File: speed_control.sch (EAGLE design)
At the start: 3 parts

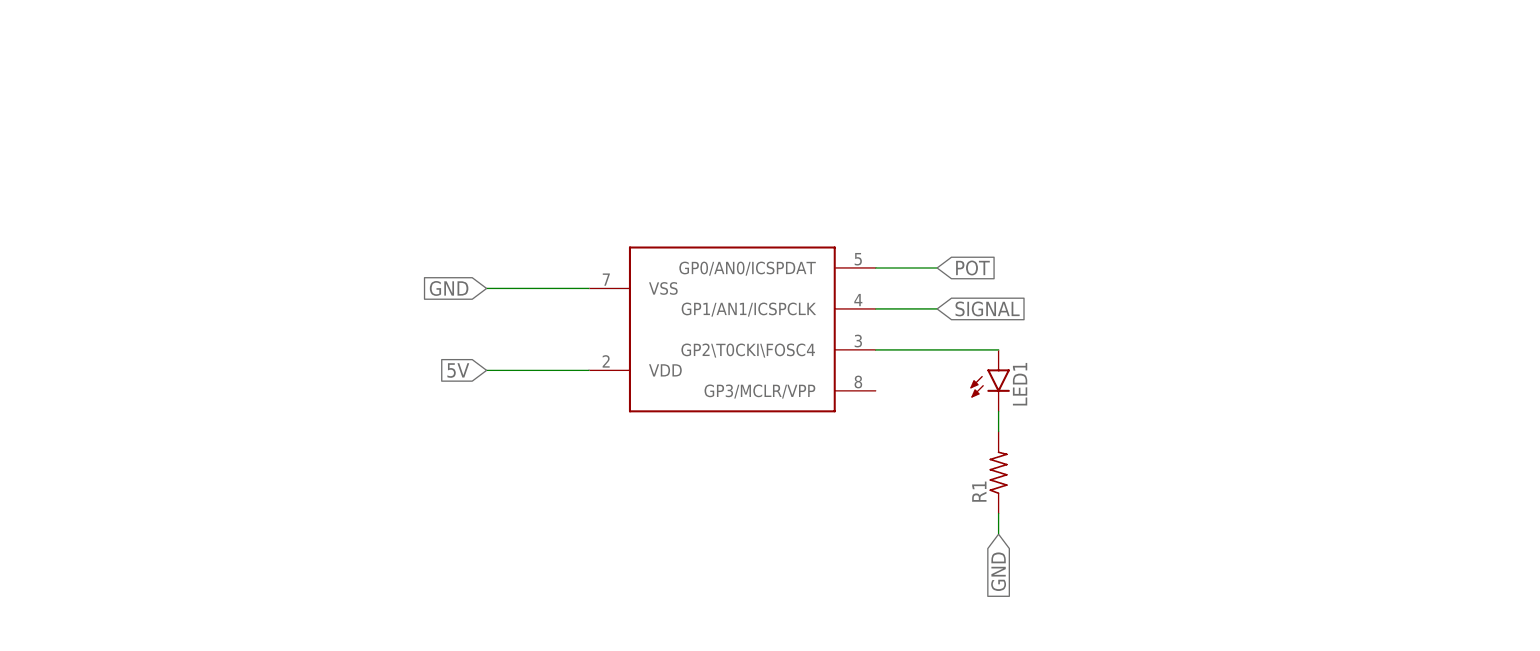
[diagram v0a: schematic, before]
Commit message: Added headers to circuit
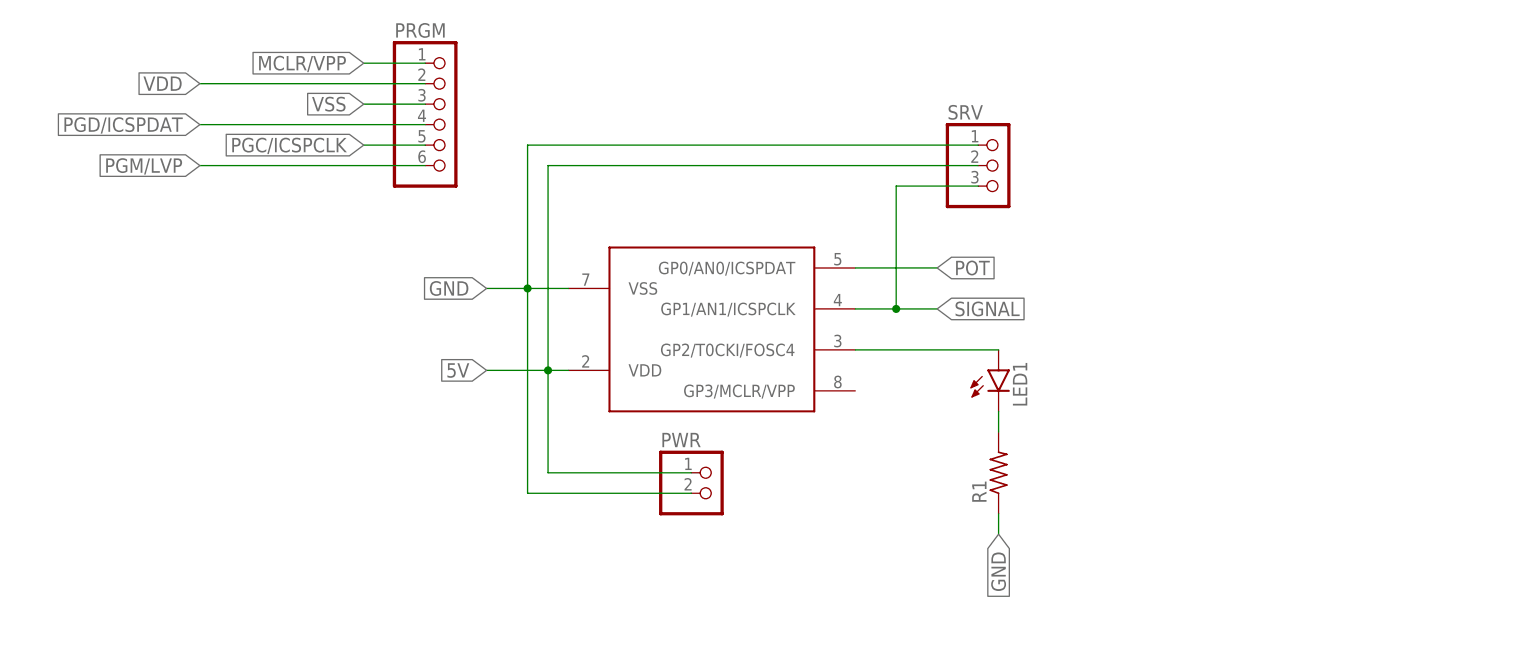
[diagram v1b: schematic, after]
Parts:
- added PRGM: (no value), pinhead:PINHD-1X6/90
- added PWR: (no value), pinhead:PINHD-1X2/90
- added SRV: (no value), pinhead:PINHD-1X3/90
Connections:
- new net MCLR/VPP: PRGM.1
- new net PGC/ICSPCLK: PRGM.5
- new net PGD/ICSPDAT: PRGM.4
- new net PGM/LVP: PRGM.6
- new net VDD: PRGM.2
- new net VSS: PRGM.3
- net 5V: now also PWR.1, SRV.2
- net GND: now also PWR.2, SRV.1
- net N$1: now also U$1.GP2/T0CKI/FOSC4; no longer U$1.GP2\T0CKI\FOSC4
- net SIGNAL: now also SRV.3
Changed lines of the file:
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@@
 </classes>
 <parts>
-<part name="U$1" library="PIC10F222" deviceset="PIC10F222" device="PIC10F222" package3d_urn="urn:adsk.eagle:package:16702925/1"/>
 <part name="LED1" library="led" library_urn="urn:adsk.eagle:library:259" deviceset="LED" device="3MM" package3d_urn="urn:adsk.eagle:package:15797/1"/>
 <part name="R1" library="rcl" library_urn="urn:adsk.eagle:library:334" deviceset="R-US_" device="0207/10" package3d_urn="urn:adsk.eagle:package:23491/2"/>
+<part name="SRV" library="pinhead" library_urn="urn:adsk.eagle:library:325" deviceset="PINHD-1X3" device="/90" package3d_urn="urn:adsk.eagle:package:22459/2"/>
+<part name="PWR" library="pinhead" library_urn="urn:adsk.eagle:library:325" deviceset="PINHD-1X2" device="/90" package3d_urn="urn:adsk.eagle:package:22437/2"/>
+<part name="PRGM" library="pinhead" library_urn="urn:adsk.eagle:library:325" deviceset="PINHD-1X6" device="/90" package3d_urn="urn:adsk.eagle:package:22475/2"/>
+<part name="U$1" library="PIC10F222" deviceset="PIC10F222" device="PIC10F222" package3d_urn="urn:adsk.eagle:package:16702925/1"/>
 </parts>
 <sheets>
@@
 </plain>
 <instances>
-<instance part="U$1" gate="G$1" x="-2.54" y="-7.62" smashed="yes"/>
 <instance part="LED1" gate="G$1" x="33.02" y="-5.08" smashed="yes">
 <attribute name="NAME" x="36.576" y="-9.652" size="1.778" layer="95" rot="R90"/>
@@
 <attribute name="VALUE" x="36.322" y="-21.59" size="1.778" layer="96" rot="R90"/>
 </instance>
+<instance part="SRV" gate="A" x="33.02" y="20.32" smashed="yes">
+<attribute name="NAME" x="26.67" y="26.035" size="1.778" layer="95"/>
+<attribute name="VALUE" x="26.67" y="12.7" size="1.778" layer="96"/>
+</instance>
+<instance part="PWR" gate="G$1" x="-2.54" y="-20.32" smashed="yes">
+<attribute name="NAME" x="-8.89" y="-14.605" size="1.778" layer="95"/>
+<attribute name="VALUE" x="-8.89" y="-25.4" size="1.778" layer="96"/>
+</instance>
+<instance part="PRGM" gate="A" x="-35.56" y="25.4" smashed="yes">
+<attribute name="NAME" x="-41.91" y="36.195" size="1.778" layer="95"/>
+<attribute name="VALUE" x="-41.91" y="15.24" size="1.778" layer="96"/>
+</instance>
+<instance part="U$1" gate="G$1" x="-2.54" y="0" smashed="yes"/>
 </instances>
 <busses>
@@
 <net name="GND" class="0">
 <segment>
+<wire x1="-20.32" y1="5.08" x2="-25.4" y2="5.08" width="0.1524" layer="91"/>
+<label x="-30.48" y="5.08" size="1.778" layer="95" rot="R180" xref="yes"/>
+<pinref part="PWR" gate="G$1" pin="2"/>
+<wire x1="-25.4" y1="5.08" x2="-30.48" y2="5.08" width="0.1524" layer="91"/>
+<wire x1="-5.08" y1="-20.32" x2="-25.4" y2="-20.32" width="0.1524" layer="91"/>
+<wire x1="-25.4" y1="-20.32" x2="-25.4" y2="5.08" width="0.1524" layer="91"/>
+<junction x="-25.4" y="5.08"/>
+<wire x1="-25.4" y1="5.08" x2="-25.4" y2="22.86" width="0.1524" layer="91"/>
+<pinref part="SRV" gate="A" pin="1"/>
+<wire x1="-25.4" y1="22.86" x2="30.48" y2="22.86" width="0.1524" layer="91"/>
 <pinref part="U$1" gate="G$1" pin="VSS"/>
-<wire x1="-17.78" y1="5.08" x2="-30.48" y2="5.08" width="0.1524" layer="91"/>
-<label x="-30.48" y="5.08" size="1.778" layer="95" rot="R180" xref="yes"/>
 </segment>
 <segment>
@@
 <net name="5V" class="0">
 <segment>
+<wire x1="-20.32" y1="-5.08" x2="-22.86" y2="-5.08" width="0.1524" layer="91"/>
+<label x="-30.48" y="-5.08" size="1.778" layer="95" rot="R180" xref="yes"/>
+<pinref part="PWR" gate="G$1" pin="1"/>
+<wire x1="-22.86" y1="-5.08" x2="-30.48" y2="-5.08" width="0.1524" layer="91"/>
+<wire x1="-5.08" y1="-17.78" x2="-22.86" y2="-17.78" width="0.1524" layer="91"/>
+<wire x1="-22.86" y1="-17.78" x2="-22.86" y2="-5.08" width="0.1524" layer="91"/>
+<junction x="-22.86" y="-5.08"/>
+<wire x1="-22.86" y1="-5.08" x2="-22.86" y2="20.32" width="0.1524" layer="91"/>
+<pinref part="SRV" gate="A" pin="2"/>
+<wire x1="-22.86" y1="20.32" x2="30.48" y2="20.32" width="0.1524" layer="91"/>
 <pinref part="U$1" gate="G$1" pin="VDD"/>
-<wire x1="-17.78" y1="-5.08" x2="-30.48" y2="-5.08" width="0.1524" layer="91"/>
-<label x="-30.48" y="-5.08" size="1.778" layer="95" rot="R180" xref="yes"/>
 </segment>
 </net>
 <net name="POT" class="0">
 <segment>
+<wire x1="15.24" y1="7.62" x2="25.4" y2="7.62" width="0.1524" layer="91"/>
+<label x="25.4" y="7.62" size="1.778" layer="95" xref="yes"/>
 <pinref part="U$1" gate="G$1" pin="GP0/AN0/ICSPDAT"/>
-<wire x1="17.78" y1="7.62" x2="25.4" y2="7.62" width="0.1524" layer="91"/>
-<label x="25.4" y="7.62" size="1.778" layer="95" xref="yes"/>
 </segment>
 </net>
 <net name="SIGNAL" class="0">
 <segment>
+<wire x1="15.24" y1="2.54" x2="20.32" y2="2.54" width="0.1524" layer="91"/>
+<label x="25.4" y="2.54" size="1.778" layer="95" xref="yes"/>
+<wire x1="20.32" y1="2.54" x2="25.4" y2="2.54" width="0.1524" layer="91"/>
+<wire x1="20.32" y1="2.54" x2="20.32" y2="17.78" width="0.1524" layer="91"/>
+<junction x="20.32" y="2.54"/>
+<pinref part="SRV" gate="A" pin="3"/>
+<wire x1="20.32" y1="17.78" x2="30.48" y2="17.78" width="0.1524" layer="91"/>
 <pinref part="U$1" gate="G$1" pin="GP1/AN1/ICSPCLK"/>
-<wire x1="17.78" y1="2.54" x2="25.4" y2="2.54" width="0.1524" layer="91"/>
-<label x="25.4" y="2.54" size="1.778" layer="95" xref="yes"/>
 </segment>
 </net>
 <net name="N$1" class="0">
 <segment>
-<pinref part="U$1" gate="G$1" pin="GP2\T0CKI\FOSC4"/>
 <pinref part="LED1" gate="G$1" pin="A"/>
-<wire x1="17.78" y1="-2.54" x2="33.02" y2="-2.54" width="0.1524" layer="91"/>
+<wire x1="15.24" y1="-2.54" x2="33.02" y2="-2.54" width="0.1524" layer="91"/>
+<pinref part="U$1" gate="G$1" pin="GP2/T0CKI/FOSC4"/>
 </segment>
 </net>
@@
 </segment>
 </net>
+<net name="MCLR/VPP" class="0">
+<segment>
+<pinref part="PRGM" gate="A" pin="1"/>
+<wire x1="-38.1" y1="33.02" x2="-45.72" y2="33.02" width="0.1524" layer="91"/>
+<label x="-45.72" y="33.02" size="1.778" layer="95" rot="R180" xref="yes"/>
+</segment>
+</net>
+<net name="VDD" class="0">
+<segment>
+<pinref part="PRGM" gate="A" pin="2"/>
+<wire x1="-38.1" y1="30.48" x2="-66.04" y2="30.48" width="0.1524" layer="91"/>
+<label x="-66.04" y="30.48" size="1.778" layer="95" rot="R180" xref="yes"/>
+</segment>
+</net>
+<net name="VSS" class="0">
+<segment>
+<pinref part="PRGM" gate="A" pin="3"/>
+<wire x1="-38.1" y1="27.94" x2="-45.72" y2="27.94" width="0.1524" layer="91"/>
+<label x="-45.72" y="27.94" size="1.778" layer="95" rot="R180" xref="yes"/>
+</segment>
+</net>
+<net name="PGD/ICSPDAT" class="0">
+<segment>
+<pinref part="PRGM" gate="A" pin="4"/>
+<wire x1="-38.1" y1="25.4" x2="-66.04" y2="25.4" width="0.1524" layer="91"/>
+<label x="-66.04" y="25.4" size="1.778" layer="95" rot="R180" xref="yes"/>
+</segment>
+</net>
+<net name="PGC/ICSPCLK" class="0">
+<segment>
+<pinref part="PRGM" gate="A" pin="5"/>
+<wire x1="-38.1" y1="22.86" x2="-45.72" y2="22.86" width="0.1524" layer="91"/>
+<label x="-45.72" y="22.86" size="1.778" layer="95" rot="R180" xref="yes"/>
+</segment>
+</net>
+<net name="PGM/LVP" class="0">
+<segment>
+<pinref part="PRGM" gate="A" pin="6"/>
+<wire x1="-38.1" y1="20.32" x2="-66.04" y2="20.32" width="0.1524" layer="91"/>
+<label x="-66.04" y="20.32" size="1.778" layer="95" rot="R180" xref="yes"/>
+</segment>
+</net>

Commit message: Added programming interface
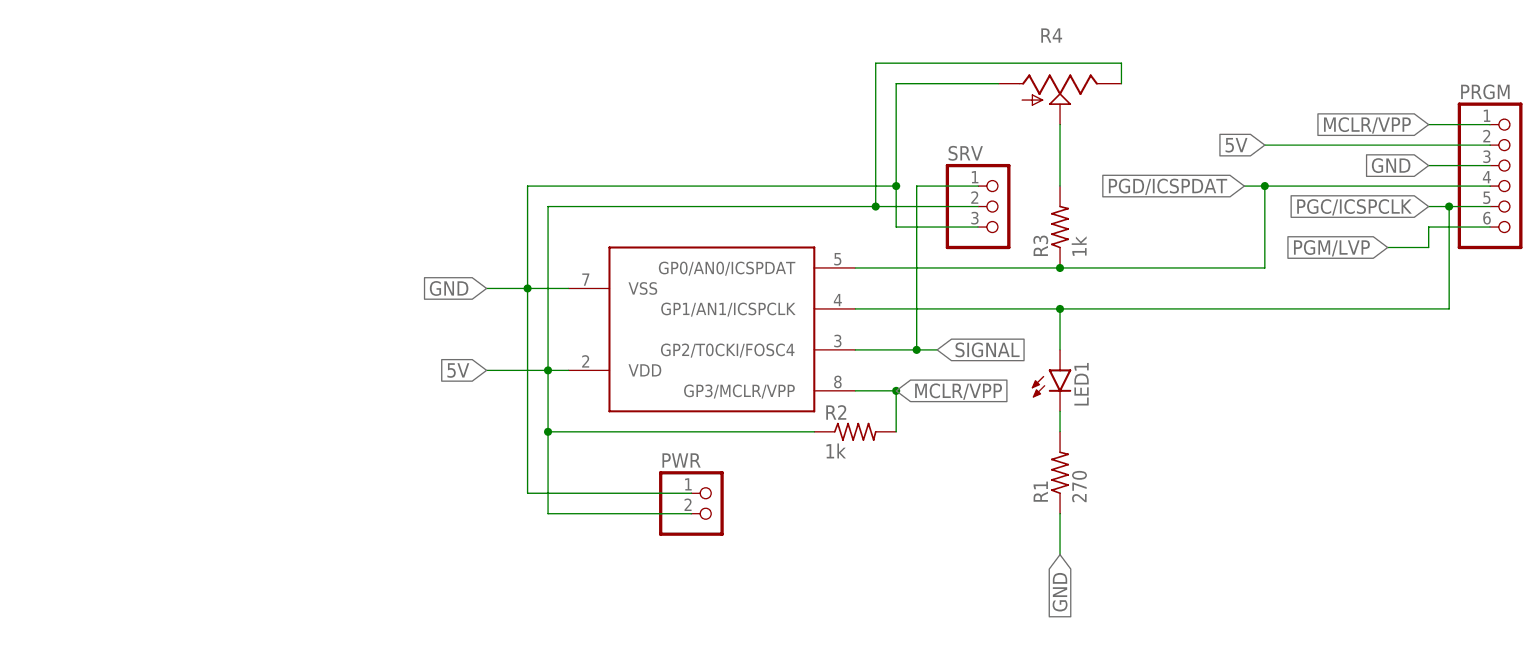
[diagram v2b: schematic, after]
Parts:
- added R2, R3: 1k, rcl:R-US_0207/10
- added R4: (no value), pot:TRIM_US-RS3
- R1: value (none) -> 270
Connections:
- removed net POT: U$1.GP0/AN0/ICSPDAT
- removed net VDD: PRGM.2
- removed net VSS: PRGM.3
- net 5V: now also PRGM.2, PWR.2, R2.1, R4.E; no longer PWR.1
- net GND: now also PRGM.3, PWR.1, R4.A, SRV.3; no longer PWR.2, SRV.1
- net MCLR/VPP: now also R2.2, U$1.GP3/MCLR/VPP
- net N$1: now also R3.2, R4.S; no longer LED1.A, U$1.GP2/T0CKI/FOSC4
- net PGC/ICSPCLK: now also LED1.A, U$1.GP1/AN1/ICSPCLK
- net PGD/ICSPDAT: now also R3.1, U$1.GP0/AN0/ICSPDAT
- net SIGNAL: now also SRV.1, U$1.GP2/T0CKI/FOSC4; no longer SRV.3, U$1.GP1/AN1/ICSPCLK
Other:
- moved on the sheet: LED1, PRGM, PWR, R1, SRV

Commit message: Layout of PCB complete
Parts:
- removed R4: (no value), pot:TRIM_US-RS3
- added POT: (no value), pinhead:PINHD-1X3
- PRGM: device pinhead:PINHD-1X6/90 -> pinhead:PINHD-1X6
- R2: value 1k -> 10k
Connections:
- net 5V: now also POT.3; no longer R4.E
- net GND: now also POT.1; no longer R4.A
- net N$1: now also POT.2; no longer R4.S
